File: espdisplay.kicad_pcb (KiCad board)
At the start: 2 copper layers, 34.3 x 30 mm, 11 parts, among them J1 PWR, J2 UReg, J3 DOut, J4 Serial, J5 IO32, SW1 RESET, SW2 BOOT, U1 ESP-WROOM-32

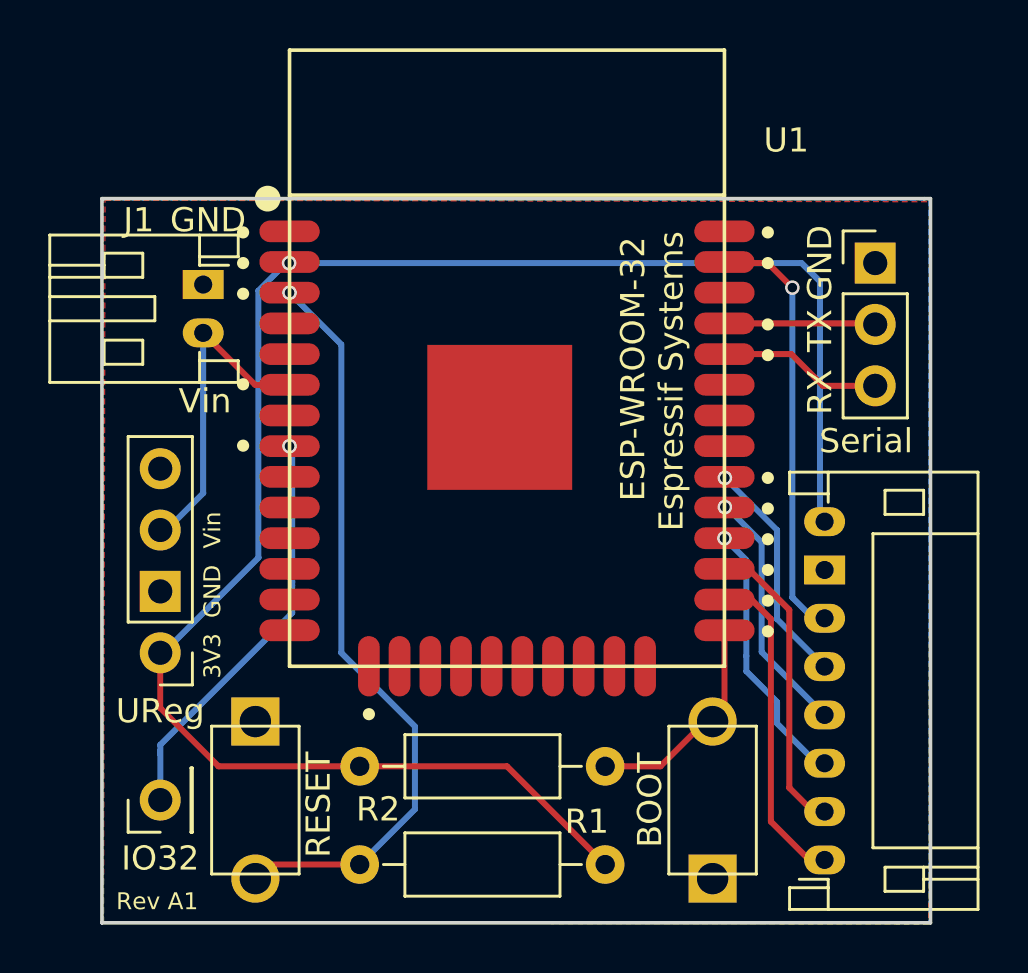
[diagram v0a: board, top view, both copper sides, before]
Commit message: Via min size
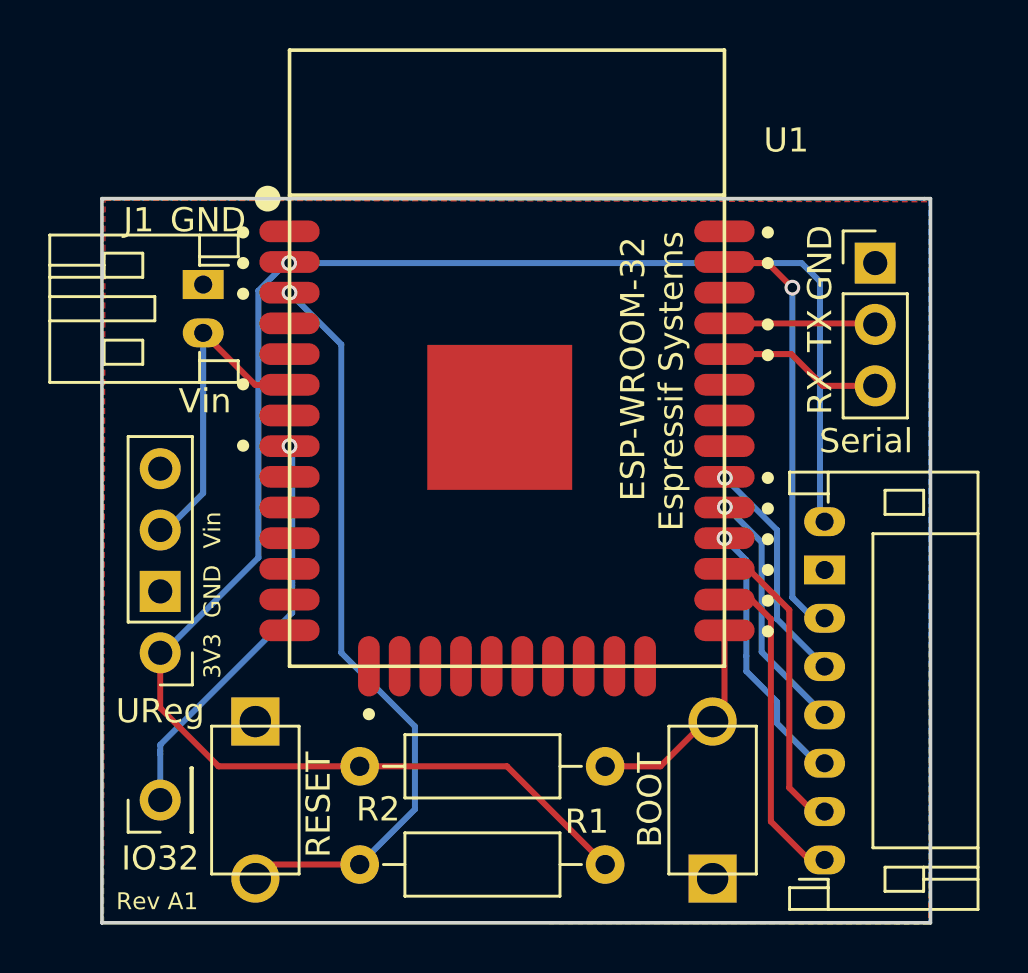
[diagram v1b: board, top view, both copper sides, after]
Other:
- net class Default: via_dia 0.6 -> 0.65
- rule via_min_size: 0.6 -> 0.65
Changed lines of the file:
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@@
     (segment_width 0.25)
     (edge_width 0.15)
-    (via_size 0.6)
+    (via_size 0.65)
     (via_drill 0.4)
-    (via_min_size 0.6)
+    (via_min_size 0.65)
     (via_min_drill 0.4)
     (uvia_size 0.3)
@@
     (clearance 0.2)
     (trace_width 0.25)
-    (via_dia 0.6)
+    (via_dia 0.65)
     (via_drill 0.4)
     (uvia_dia 0.3)
@@
   (segment (start 177.3465 105.263) (end 177.537 105.4535) (width 0.25) (layer B.Cu) (net 3) (status 30))
   (segment (start 155.3755 94.752) (end 155.3925 94.735) (width 0.25) (layer F.Cu) (net 3) (status 30))
-  (via (at 155.3755 94.752) (size 0.6) (drill 0.4) (layers F.Cu B.Cu) (net 3) (status 30))
+  (via (at 155.3755 94.752) (size 0.65) (drill 0.4) (layers F.Cu B.Cu) (net 3) (status 30))
   (segment (start 155.3925 94.735) (end 155.3925 94.709) (width 0.25) (layer F.Cu) (net 3) (status 30))
   (segment (start 155.5025 94.625) (end 155.3925 94.709) (width 0.25) (layer F.Cu) (net 3) (status 80030))
@@
   (segment (start 175.1875 94.752) (end 173.4355 94.752) (width 0.25) (layer F.Cu) (net 4))
   (segment (start 177.062 109.4535) (end 176.2035 108.595) (width 0.25) (layer B.Cu) (net 4))
-  (via (at 176.2035 95.768) (size 0.6) (drill 0.4) (layers F.Cu B.Cu) (net 4))
+  (via (at 176.2035 95.768) (size 0.65) (drill 0.4) (layers F.Cu B.Cu) (net 4))
   (segment (start 176.2035 108.595) (end 176.2035 95.768) (width 0.25) (layer B.Cu) (net 4))
   (segment (start 177.537 109.4535) (end 177.062 109.4535) (width 0.25) (layer B.Cu) (net 4))
   (segment (start 173.3925 103.599) (end 173.3925 103.625) (width 0.25) (layer F.Cu) (net 5) (status 30))
   (segment (start 173.3925 103.625) (end 173.4095 103.642) (width 0.25) (layer F.Cu) (net 5) (status 30))
-  (via (at 173.4095 103.642) (size 0.6) (drill 0.4) (layers F.Cu B.Cu) (net 5) (status 30))
+  (via (at 173.4095 103.642) (size 0.65) (drill 0.4) (layers F.Cu B.Cu) (net 5) (status 30))
   (segment (start 173.4095 103.642) (end 175.5685 105.801) (width 0.25) (layer B.Cu) (net 5))
   (segment (start 175.5685 105.801) (end 175.5685 109.485) (width 0.25) (layer B.Cu) (net 5))
@@
   (segment (start 174.9335 106.309) (end 174.9335 110.85) (width 0.25) (layer B.Cu) (net 6))
   (segment (start 173.3925 104.8655) (end 173.4095 104.8485) (width 0.25) (layer F.Cu) (net 6) (status 30))
-  (via (at 173.4095 104.8485) (size 0.6) (drill 0.4) (layers F.Cu B.Cu) (net 6) (status 30))
+  (via (at 173.4095 104.8485) (size 0.65) (drill 0.4) (layers F.Cu B.Cu) (net 6) (status 30))
   (segment (start 173.3925 104.869) (end 173.3925 104.8655) (width 0.25) (layer F.Cu) (net 6) (status 30))
   (segment (start 177.537 115.4535) (end 177.22 115.4535) (width 0.25) (layer B.Cu) (net 7))
@@
   (segment (start 174.2985 111.643) (end 175.5685 112.913) (width 0.25) (layer B.Cu) (net 7))
   (segment (start 174.2985 111.008) (end 174.2985 111.643) (width 0.25) (layer B.Cu) (net 7))
-  (via (at 173.3925 106.139) (size 0.6) (drill 0.4) (layers F.Cu B.Cu) (net 7))
+  (via (at 173.3925 106.139) (size 0.65) (drill 0.4) (layers F.Cu B.Cu) (net 7))
   (segment (start 174.2985 107.045) (end 174.2985 111.008) (width 0.25) (layer B.Cu) (net 7))
   (segment (start 174.2985 107.045) (end 173.3925 106.139) (width 0.25) (layer B.Cu) (net 7))
@@
   (segment (start 160.5825 117.358) (end 158.2965 119.644) (width 0.25) (layer B.Cu) (net 10) (status 20))
   (segment (start 160.5825 113.929) (end 160.5825 117.358) (width 0.25) (layer B.Cu) (net 10))
-  (via (at 155.3925 95.979) (size 0.6) (drill 0.4) (layers F.Cu B.Cu) (net 10) (status 30))
+  (via (at 155.3925 95.979) (size 0.65) (drill 0.4) (layers F.Cu B.Cu) (net 10) (status 30))
   (segment (start 155.3925 95.979) (end 157.5345 98.121) (width 0.25) (layer B.Cu) (net 10))
   (segment (start 157.5345 98.121) (end 157.5345 110.881) (width 0.25) (layer B.Cu) (net 10))
@@
   (segment (start 150.0415 114.945) (end 150.0415 115.072) (width 0.25) (layer B.Cu) (net 37))
   (segment (start 155.5025 108.087) (end 155.5025 107.96) (width 0.25) (layer B.Cu) (net 37))
-  (via (at 155.3925 102.329) (size 0.6) (drill 0.4) (layers F.Cu B.Cu) (net 37))
+  (via (at 155.3925 102.329) (size 0.65) (drill 0.4) (layers F.Cu B.Cu) (net 37))
   (segment (start 155.5025 102.439) (end 155.5025 107.96) (width 0.25) (layer B.Cu) (net 37))
   (segment (start 155.5025 102.439) (end 155.3925 102.329) (width 0.25) (layer B.Cu) (net 37))

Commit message: cleanup and pwr trace width
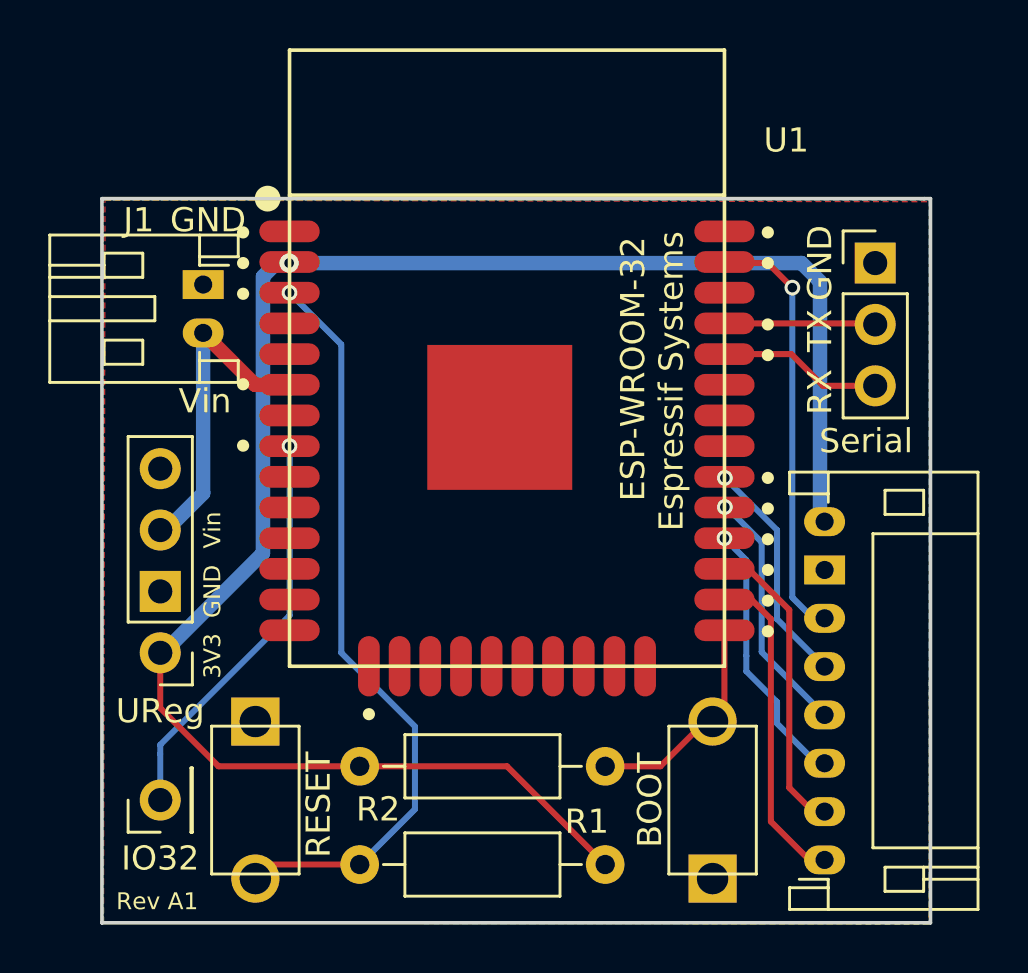
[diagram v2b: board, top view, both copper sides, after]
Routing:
- net Net-(R2-Pad2): track 10.2 -> 9.25 mm
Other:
- net class PWR added: clearance 0.2, trace_width 0.6, via_dia 0.8, via_drill 0.4
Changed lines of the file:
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@@
     (links 28)
     (no_connects 0)
-    (area 143.5945 83.49 185.862 122.132001)
+    (area 147.553499 92.009999 181.993501 122.132001)
     (thickness 1.6)
     (drawings 38)
-    (tracks 93)
+    (tracks 79)
     (zones 0)
     (modules 11)
@@
   (layers
     (0 F.Cu mixed)
-    (31 B.Cu mixed hide)
+    (31 B.Cu mixed)
     (32 B.Adhes user)
     (33 F.Adhes user)
@@
     (uvia_dia 0.3)
     (uvia_drill 0.1)
-    (add_net +3V3)
     (add_net /BUSY)
     (add_net /CLK)
@@
     (add_net /IO32)
     (add_net /RST)
-    (add_net /Vin)
-    (add_net GND)
     (add_net "Net-(J2-Pad4)")
     (add_net "Net-(J4-Pad2)")
@@
     (add_net "Net-(U1-Pad7)")
     (add_net "Net-(U1-Pad9)")
+  )
+  (net_class PWR ""
+    (clearance 0.2)
+    (trace_width 0.6)
+    (via_dia 0.8)
+    (via_drill 0.4)
+    (uvia_dia 0.3)
+    (uvia_drill 0.1)
+    (add_net +3V3)
+    (add_net /Vin)
+    (add_net GND)
   )
   (module Symbols:OSHW-Logo_7.5x8mm_SilkScreen (layer B.Cu)
@@
     (effects (font (size 1 1) (thickness 0.15)))
   )
-  (segment (start 150.0415 105.801) (end 150.2955 105.801) (width 0.25) (layer B.Cu) (net 1))
-  (segment (start 150.2955 105.801) (end 151.8195 104.277) (width 0.25) (layer B.Cu) (net 1))
-  (segment (start 151.8195 97.641) (end 151.8195 104.277) (width 0.25) (layer B.Cu) (net 1) (status 10))
-  (segment (start 155.3925 99.789) (end 153.9675 99.789) (width 0.25) (layer F.Cu) (net 1) (status 10))
-  (segment (start 153.9675 99.789) (end 151.8195 97.641) (width 0.25) (layer F.Cu) (net 1) (status 20))
-  (segment (start 155.3755 94.752) (end 155.2485 94.752) (width 0.25) (layer B.Cu) (net 3))
-  (segment (start 155.2485 94.752) (end 154.1055 95.895) (width 0.25) (layer B.Cu) (net 3))
-  (segment (start 150.0415 110.881) (end 150.1685 110.881) (width 0.25) (layer B.Cu) (net 3))
-  (segment (start 150.1685 110.881) (end 154.1055 106.944) (width 0.25) (layer B.Cu) (net 3))
-  (segment (start 154.1055 95.895) (end 154.1055 106.944) (width 0.25) (layer B.Cu) (net 3))
-  (segment (start 177.3465 95.514) (end 176.5845 94.752) (width 0.25) (layer B.Cu) (net 3))
-  (segment (start 177.3465 95.514) (end 177.3465 105.263) (width 0.25) (layer B.Cu) (net 3))
+  (segment (start 150.2955 105.801) (end 151.8195 104.277) (width 0.6) (layer B.Cu) (net 1))
+  (segment (start 151.8195 97.641) (end 151.8195 104.277) (width 0.6) (layer B.Cu) (net 1) (status 10))
+  (segment (start 155.3925 99.789) (end 153.9675 99.789) (width 0.6) (layer F.Cu) (net 1) (status 10))
+  (segment (start 153.9675 99.789) (end 151.8195 97.641) (width 0.6) (layer F.Cu) (net 1) (status 20))
+  (segment (start 155.3755 94.761289) (end 154.843791 94.761289) (width 0.6) (layer B.Cu) (net 3))
+  (segment (start 154.843791 94.761289) (end 154.292498 95.312582) (width 0.6) (layer B.Cu) (net 3))
+  (segment (start 154.292498 95.312582) (end 154.292498 106.757002) (width 0.6) (layer B.Cu) (net 3))
+  (segment (start 154.292498 106.757002) (end 150.1685 110.881) (width 0.6) (layer B.Cu) (net 3))
+  (segment (start 177.3465 95.514) (end 177.3465 105.263) (width 0.6) (layer B.Cu) (net 3))
+  (segment (start 155.3755 94.752) (end 176.5845 94.752) (width 0.6) (layer B.Cu) (net 3))
+  (segment (start 177.3465 95.514) (end 176.5845 94.752) (width 0.6) (layer B.Cu) (net 3))
   (segment (start 158.2965 115.58) (end 152.4545 115.58) (width 0.25) (layer F.Cu) (net 3) (status 10))
   (segment (start 150.0415 113.167) (end 150.0415 110.881) (width 0.25) (layer F.Cu) (net 3))
@@
   (segment (start 158.2965 115.58) (end 164.3925 115.58) (width 0.25) (layer F.Cu) (net 3) (status 10))
   (segment (start 164.3925 115.58) (end 168.4565 119.644) (width 0.25) (layer F.Cu) (net 3))
-  (segment (start 155.3755 94.752) (end 176.5845 94.752) (width 0.25) (layer B.Cu) (net 3))
-  (segment (start 177.3465 105.263) (end 177.537 105.4535) (width 0.25) (layer B.Cu) (net 3) (status 30))
-  (segment (start 155.3755 94.752) (end 155.3925 94.735) (width 0.25) (layer F.Cu) (net 3) (status 30))
-  (via (at 155.3755 94.752) (size 0.65) (drill 0.4) (layers F.Cu B.Cu) (net 3) (status 30))
-  (segment (start 155.3925 94.735) (end 155.3925 94.709) (width 0.25) (layer F.Cu) (net 3) (status 30))
-  (segment (start 155.5025 94.625) (end 155.3925 94.709) (width 0.25) (layer F.Cu) (net 3) (status 80030))
+  (via (at 155.3755 94.752) (size 0.8) (drill 0.4) (layers F.Cu B.Cu) (net 3) (status 30))
   (segment (start 176.2035 95.768) (end 175.1875 94.752) (width 0.25) (layer F.Cu) (net 4))
   (segment (start 175.1875 94.752) (end 173.4355 94.752) (width 0.25) (layer F.Cu) (net 4))
@@
   (segment (start 155.3925 95.979) (end 157.5345 98.121) (width 0.25) (layer B.Cu) (net 10))
   (segment (start 157.5345 98.121) (end 157.5345 110.881) (width 0.25) (layer B.Cu) (net 10))
-  (segment (start 155.5025 95.895) (end 155.3925 95.979) (width 0.25) (layer F.Cu) (net 10) (status 80030))
   (segment (start 172.9015 113.727) (end 172.5955 113.727) (width 0.25) (layer F.Cu) (net 11) (status 30))
   (segment (start 172.5955 113.727) (end 170.7425 115.58) (width 0.25) (layer F.Cu) (net 11) (status 10))
@@
   (segment (start 173.3925 109.949) (end 173.3925 113.236) (width 0.25) (layer F.Cu) (net 11) (status 20))
   (segment (start 173.3925 113.236) (end 172.9015 113.727) (width 0.25) (layer F.Cu) (net 11) (status 30))
-  (segment (start 168.4565 115.58) (end 169.2185 115.58) (width 0.25) (layer F.Cu) (net 11) (status 30))
-  (segment (start 173.0115 113.617) (end 172.9015 113.727) (width 0.25) (layer F.Cu) (net 11) (status 30))
   (segment (start 172.9015 113.727) (end 172.9015 113.675) (width 0.25) (layer F.Cu) (net 11) (status 80030))
   (segment (start 173.3925 97.249) (end 179.5895 97.249) (width 0.25) (layer F.Cu) (net 12) (status 30))
@@
   (segment (start 176.1605 98.519) (end 177.4735 99.832) (width 0.25) (layer F.Cu) (net 13))
   (segment (start 177.4735 99.832) (end 179.6325 99.832) (width 0.25) (layer F.Cu) (net 13))
-  (segment (start 155.5025 108.2775) (end 155.5025 109.23) (width 0.25) (layer B.Cu) (net 37))
-  (segment (start 155.5025 109.23) (end 150.0415 114.691) (width 0.25) (layer B.Cu) (net 37))
-  (segment (start 155.5025 108.2775) (end 155.5025 108.087) (width 0.25) (layer B.Cu) (net 37))
-  (segment (start 150.0415 116.977) (end 150.0415 115.072) (width 0.25) (layer B.Cu) (net 37) (status 10))
-  (segment (start 150.0415 114.691) (end 150.0415 114.945) (width 0.25) (layer B.Cu) (net 37))
-  (segment (start 150.0415 114.945) (end 150.0415 115.072) (width 0.25) (layer B.Cu) (net 37))
-  (segment (start 155.5025 108.087) (end 155.5025 107.96) (width 0.25) (layer B.Cu) (net 37))
+  (segment (start 155.393912 102.330412) (end 155.393912 109.338588) (width 0.25) (layer B.Cu) (net 37))
+  (segment (start 155.393912 109.338588) (end 150.0415 114.691) (width 0.25) (layer B.Cu) (net 37))
+  (segment (start 150.0415 114.691) (end 150.0415 115.072) (width 0.25) (layer B.Cu) (net 37))
+  (segment (start 150.0415 115.072) (end 150.0415 116.977) (width 0.25) (layer B.Cu) (net 37))
   (via (at 155.3925 102.329) (size 0.65) (drill 0.4) (layers F.Cu B.Cu) (net 37))
-  (segment (start 155.5025 102.439) (end 155.5025 107.96) (width 0.25) (layer B.Cu) (net 37))
-  (segment (start 155.5025 102.439) (end 155.3925 102.329) (width 0.25) (layer B.Cu) (net 37))
   (zone (net 2) (net_name GND) (layer F.Cu) (hatch edge 0.508)
     (connect_pads thru_hole_only (clearance 0.508))
